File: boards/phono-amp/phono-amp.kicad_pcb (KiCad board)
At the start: 2 copper layers, 28 parts, among them J1 Conn_Coaxial, J2 Conn_01x06_Male, J3 Conn_Coaxial, U1 6DJ8

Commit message: layout underway
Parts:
- moved J2 173.4 mm to (72.4, 65.8), turned to 90 degrees
- moved R12 94.9 mm to (170.2, 135.9), turned to 90 degrees
- moved C2 56.4 mm to (152.4, 87.6)
- moved R6B1 54.2 mm to (152.4, 76.2), turned to 90 degrees
- moved R6A1 42.6 mm to (160.0, 66.0), turned to 270 degrees
- moved C7 40.2 mm to (95.2, 80.0), turned to 270 degrees
- moved R7 39.2 mm to (145.8, 77.5), turned to 90 degrees
- moved R5 35.4 mm to (116.8, 69.8), turned to 270 degrees
- moved R8 33.6 mm to (139.7, 81.3)
- moved R11 31.4 mm to (195.6, 123.2)
- moved C4 31.4 mm to (184.2, 101.6)
- moved C6 31.4 mm to (154.9, 108.0)
- moved R1 31.4 mm to (71.1, 118.1)
- moved R10 31.4 mm to (163.8, 99.1)
- moved R2 31.4 mm to (95.2, 102.9)
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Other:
- board outline added: 152.4 x 115.6 mm

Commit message: Amp PCB done?
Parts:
- added H1: MountingHole_Pad, MountingHole:MountingHole_4.3mm_M4_ISO7380_Pad, F.Cu at (74.9, 41.9)
- added H2: MountingHole_Pad, MountingHole:MountingHole_4.3mm_M4_ISO7380_Pad, F.Cu at (217.2, 41.9)
- added H3: MountingHole_Pad, MountingHole:MountingHole_4.3mm_M4_ISO7380_Pad, F.Cu at (74.9, 147.3)
- added H4: MountingHole_Pad, MountingHole:MountingHole_4.3mm_M4_ISO7380_Pad, F.Cu at (217.2, 147.3)
- added H5: MountingHole_Pad, MountingHole:MountingHole_4.3mm_M4_ISO7380_Pad, F.Cu at (74.9, 72.4)
- added JP1: 6DJ8, Connector_PinHeader_2.54mm:PinHeader_1x03_P2.54mm_Vertical, F.Cu at (127.0, 102.9)
- J1: value Conn_Coaxial -> INPUT
- J2: value Conn_01x06_Male -> POWER
- J3: value Conn_Coaxial -> OUTPUT
- R5: value 82k5 1/4W 1% -> 82.5k
- R6A1: value 10k7 1/4W 1% -> 10k
- R6B1: value 100 1/4W 1% -> 100
- R7: value 470k 1/4W -> 470k
- R8: value 500R 1/4W -> 500
- moved J2 84.6 mm to (99.1, 146.1), turned to 0 degrees
- moved R12 68.6 mm to (101.6, 133.3), turned to 0 degrees
- moved R6A1 40.8 mm to (120.7, 76.8), turned to 90 degrees
- moved R6B1 38.7 mm to (114.9, 66.7), turned to 270 degrees
- moved C1A1 35.0 mm to (151.8, 67.3)
- moved C3 34.9 mm to (163.2, 77.5)
- moved C1B1 34.4 mm to (143.5, 67.3)
- moved C1C1 33.1 mm to (135.9, 67.3)
- moved C2 32.0 mm to (127.6, 67.3), turned to 270 degrees
- moved R7 17.6 mm to (149.9, 94.6), turned to 0 degrees
- moved R10 17.3 mm to (158.8, 115.6), turned to 90 degrees
- moved R2 15.9 mm to (111.1, 102.9)
- moved R11 15.8 mm to (185.4, 111.1), turned to 0 degrees
- moved R3 15.7 mm to (95.9, 113.0), turned to 0 degrees
- moved R1 15.4 mm to (73.0, 102.9), turned to 0 degrees
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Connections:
- U1 pad 10: (no net) -> Net-(JP1-Pad2)
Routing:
- net Earth_Protective: track 0.00 -> 344.7 mm
- net VBUS: track 0.00 -> 286.9 mm
- net Net-(C2-Pad1): track 0.00 -> 61.2 mm
- net Net-(C4-Pad2): track 0.00 -> 52.8 mm
- net GND: track 0.00 -> 48.4 mm
- net Net-(J2-Pad6): track 0.00 -> 40.8 mm
- net Net-(J2-Pad4): track 0.00 -> 40.5 mm
- net Net-(C4-Pad1): track 0.00 -> 38.5 mm
- net Net-(C1A1-Pad1): track 0.00 -> 35.5 mm
- net Net-(C6-Pad1): track 0.00 -> 34.9 mm
- net Net-(J1-Pad1): track 0.00 -> 26.7 mm
- net Net-(C5-Pad1): track 0.00 -> 24.0 mm
- net Net-(C7-Pad1): track 0.00 -> 23.6 mm
- net Net-(C3-Pad1): track 0.00 -> 19.0 mm
- net Net-(R8-Pad1): track 0.00 -> 18.4 mm
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- added copper zone on B.Cu, net GND
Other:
- board text added: "6DJ8 Phono Stage Design: RJM Audio"
- board text added: "PCB: E. Hazen 2021-05-02"

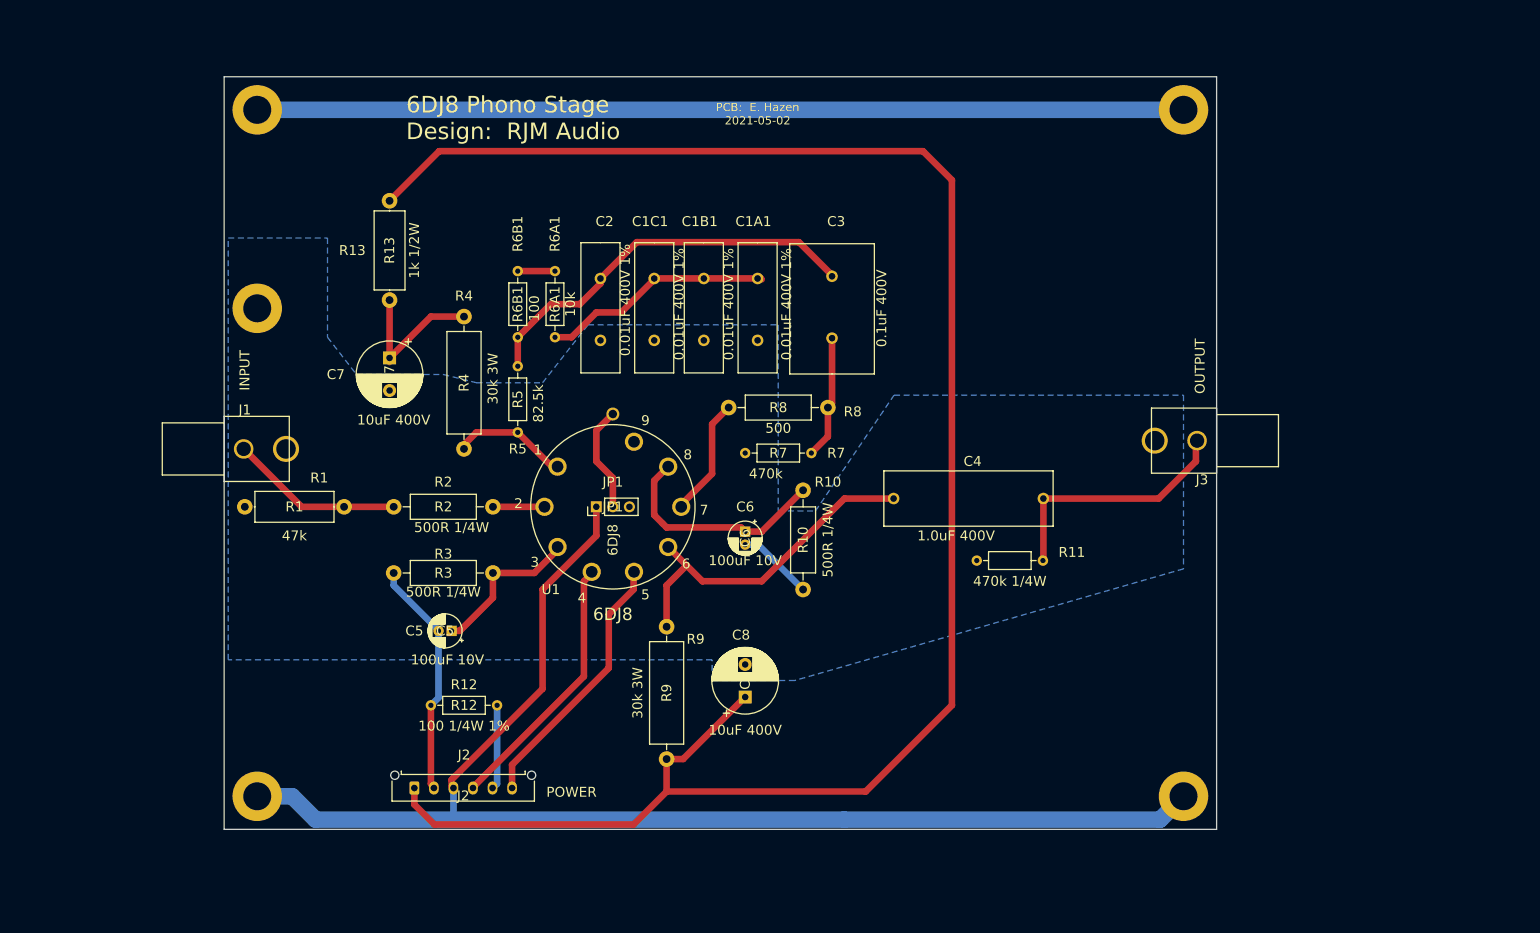
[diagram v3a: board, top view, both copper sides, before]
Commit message: resize boards
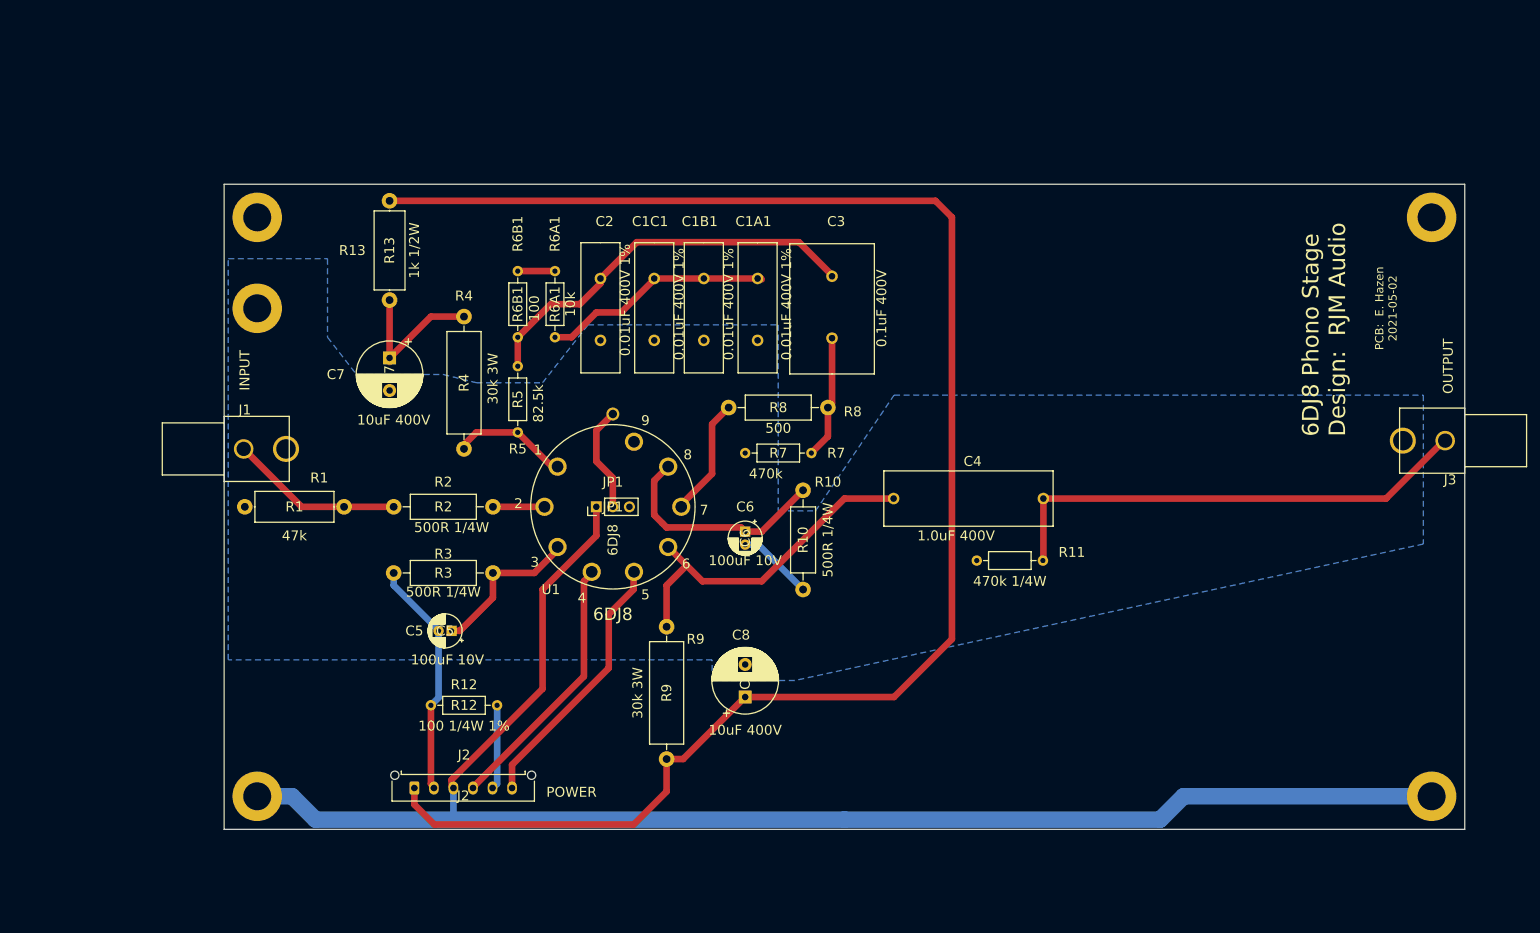
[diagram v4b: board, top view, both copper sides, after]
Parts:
- moved H2 41.5 mm to (255.3, 58.4)
- moved H4 38.1 mm to (255.3, 147.3)
- moved J3 38.1 mm to (260.4, 92.7)
- moved H1 16.5 mm to (74.9, 58.4)
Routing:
- net Earth_Protective: track 344.7 -> 240.6 mm
- net Net-(C4-Pad1): track 38.5 -> 74.8 mm
- net VBUS: track 286.9 -> 253.3 mm
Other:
- board size 152.4 x 115.6 mm -> 190.5 x 99.1 mm
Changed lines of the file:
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@@
     (thickness 1.6)
     (drawings 6)
-    (tracks 110)
+    (tracks 108)
     (zones 0)
     (modules 34)
@@
   )
   (setup
-    (last_trace_width 0.25)
+    (last_trace_width 1.016)
     (user_trace_width 0.381)
     (user_trace_width 0.635)
@@
     (add_net "Net-(R8-Pad1)")
     (add_net VBUS)
+  )
+  (module my-connectors:rca-single-klpx (layer F.Cu)
+    (at 260.35 92.71 180)
+    (fp_text reference J3 (at 2.25 -6) (layer F.SilkS)
+      (effects (font (size 1.524 1.524) (thickness 0.15)))
+    )
+    (fp_text value OUTPUT (at 2.54 11.43 90) (layer F.SilkS)
+      (effects (font (size 1.524 1.524) (thickness 0.15)))
+    )
+    (fp_line (start 0 -5) (end 0 5) (layer F.SilkS) (width 0.12))
+    (fp_line (start 0 5) (end 10 5) (layer F.SilkS) (width 0.12))
+    (fp_line (start 10 -5) (end 0 -5) (layer F.SilkS) (width 0.12))
+    (fp_line (start 10 -5) (end 10 5) (layer F.SilkS) (width 0.12))
+    (fp_line (start 0 -4) (end -9.5 -4) (layer F.SilkS) (width 0.12))
+    (fp_line (start -9.5 -4) (end -9.5 4) (layer F.SilkS) (width 0.12))
+    (fp_line (start -9.5 4) (end 0 4) (layer F.SilkS) (width 0.12))
+    (pad 2 thru_hole circle (at 9.5 0 180) (size 4 4) (drill 3) (layers *.Cu *.Mask)
+      (net 1 GND))
+    (pad 1 thru_hole circle (at 3 0 180) (size 3 3) (drill 2.2) (layers *.Cu *.Mask)
+      (net 4 "Net-(C4-Pad1)"))
   )
   (module my-capacitors:CAP_L20_W6.4_P9.5 (layer F.Cu)
@@
     )
   )
-  (module my-connectors:rca-single-klpx (layer F.Cu)
-    (at 222.25 92.71 180)
-    (fp_text reference J3 (at 2.25 -6) (layer F.SilkS)
-      (effects (font (size 1.524 1.524) (thickness 0.15)))
-    )
-    (fp_text value OUTPUT (at 2.54 11.43 90) (layer F.SilkS)
-      (effects (font (size 1.524 1.524) (thickness 0.15)))
-    )
-    (fp_line (start 0 -5) (end 0 5) (layer F.SilkS) (width 0.12))
-    (fp_line (start 0 5) (end 10 5) (layer F.SilkS) (width 0.12))
-    (fp_line (start 10 -5) (end 0 -5) (layer F.SilkS) (width 0.12))
-    (fp_line (start 10 -5) (end 10 5) (layer F.SilkS) (width 0.12))
-    (fp_line (start 0 -4) (end -9.5 -4) (layer F.SilkS) (width 0.12))
-    (fp_line (start -9.5 -4) (end -9.5 4) (layer F.SilkS) (width 0.12))
-    (fp_line (start -9.5 4) (end 0 4) (layer F.SilkS) (width 0.12))
-    (pad 2 thru_hole circle (at 9.5 0 180) (size 4 4) (drill 3) (layers *.Cu *.Mask)
-      (net 1 GND))
-    (pad 1 thru_hole circle (at 3 0 180) (size 3 3) (drill 2.2) (layers *.Cu *.Mask)
-      (net 4 "Net-(C4-Pad1)"))
-  )
   (module Resistor_THT:R_Axial_DIN0414_L11.9mm_D4.5mm_P15.24mm_Horizontal (layer F.Cu)
     (at 73.025 102.87)
@@
   )
   (module MountingHole:MountingHole_4.3mm_M4_ISO7380_Pad (layer F.Cu)
-    (at 74.93 41.91)
+    (at 74.93 58.42)
     (descr "Mounting Hole 4.3mm, M4, ISO7380")
     (tags "mounting hole 4.3mm m4 iso7380")
@@
   )
   (module MountingHole:MountingHole_4.3mm_M4_ISO7380_Pad (layer F.Cu)
-    (at 217.17 41.91)
+    (at 255.27 58.42)
     (descr "Mounting Hole 4.3mm, M4, ISO7380")
     (tags "mounting hole 4.3mm m4 iso7380")
@@
   )
   (module MountingHole:MountingHole_4.3mm_M4_ISO7380_Pad (layer F.Cu)
-    (at 217.17 147.32)
+    (at 255.27 147.32)
     (descr "Mounting Hole 4.3mm, M4, ISO7380")
     (tags "mounting hole 4.3mm m4 iso7380")
@@
     )
   )
-  (gr_text "PCB:  E. Hazen\n2021-05-02" (at 151.765 42.545) (layer F.SilkS)
+  (gr_text "PCB:  E. Hazen\n2021-05-02" (at 248.285 72.39 90) (layer F.SilkS)
     (effects (font (size 1.27 1.27) (thickness 0.2032)))
   )
-  (gr_text "6DJ8 Phono Stage\nDesign:  RJM Audio" (at 97.79 43.18) (layer F.SilkS)
+  (gr_text "6DJ8 Phono Stage\nDesign:  RJM Audio" (at 238.76 92.075 90) (layer F.SilkS)
     (effects (font (size 2.54 2.54) (thickness 0.2032)) (justify left))
   )
-  (gr_line (start 222.25 36.83) (end 69.85 36.83) (layer Edge.Cuts) (width 0.05))
-  (gr_line (start 222.25 152.4) (end 222.25 36.83) (layer Edge.Cuts) (width 0.05))
-  (gr_line (start 69.85 152.4) (end 222.25 152.4) (layer Edge.Cuts) (width 0.05))
-  (gr_line (start 69.85 36.83) (end 69.85 152.4) (layer Edge.Cuts) (width 0.05))
+  (gr_line (start 260.35 53.34) (end 69.85 53.34) (layer Edge.Cuts) (width 0.05))
+  (gr_line (start 260.35 152.4) (end 260.35 53.34) (layer Edge.Cuts) (width 0.05))
+  (gr_line (start 69.85 152.4) (end 260.35 152.4) (layer Edge.Cuts) (width 0.05))
+  (gr_line (start 69.85 53.34) (end 69.85 152.4) (layer Edge.Cuts) (width 0.05))
   (segment (start 102.775 121.92) (end 102.775 132.175) (width 1.016) (layer B.Cu) (net 1))
   (segment (start 102.775 132.175) (end 101.6 133.35) (width 1.016) (layer B.Cu) (net 1))
@@
   (segment (start 162.56 87.63) (end 162.56 92.075) (width 1.016) (layer F.Cu) (net 3))
   (segment (start 162.56 92.075) (end 160.02 94.615) (width 1.016) (layer F.Cu) (net 3))
-  (segment (start 195.65 101.6) (end 213.36 101.6) (width 1.016) (layer F.Cu) (net 4))
-  (segment (start 213.36 101.6) (end 219.075 95.885) (width 1.016) (layer F.Cu) (net 4))
-  (segment (start 219.075 95.885) (end 219.075 92.71) (width 1.016) (layer F.Cu) (net 4))
   (segment (start 195.65 101.6) (end 195.65 111.055) (width 1.016) (layer F.Cu) (net 4))
   (segment (start 195.65 111.055) (end 195.58 111.125) (width 1.016) (layer F.Cu) (net 4))
+  (segment (start 195.65 101.6) (end 248.285 101.6) (width 1.016) (layer F.Cu) (net 4))
+  (segment (start 248.285 101.6) (end 257.175 92.71) (width 1.016) (layer F.Cu) (net 4))
   (segment (start 143.292933 114.3) (end 152.4 114.3) (width 1.016) (layer F.Cu) (net 5))
   (segment (start 152.4 114.3) (end 165.1 101.6) (width 1.016) (layer F.Cu) (net 5))
@@
   (segment (start 137.795 141.605) (end 140.335 141.605) (width 1.016) (layer F.Cu) (net 9))
   (segment (start 140.335 141.605) (end 149.86 132.08) (width 1.016) (layer F.Cu) (net 9))
-  (segment (start 95.25 55.88) (end 102.87 48.26) (width 1.016) (layer F.Cu) (net 9))
-  (segment (start 102.87 48.26) (end 177.165 48.26) (width 1.016) (layer F.Cu) (net 9))
-  (segment (start 177.165 48.26) (end 181.61 52.705) (width 1.016) (layer F.Cu) (net 9))
-  (segment (start 181.61 52.705) (end 181.61 133.35) (width 1.016) (layer F.Cu) (net 9))
-  (segment (start 168.37301 146.58699) (end 137.795 146.58699) (width 1.016) (layer F.Cu) (net 9))
-  (segment (start 181.61 133.35) (end 168.37301 146.58699) (width 1.016) (layer F.Cu) (net 9))
   (segment (start 99.06 148.59) (end 99.06 146.05) (width 1.016) (layer F.Cu) (net 9))
+  (segment (start 95.25 55.88) (end 179.07 55.88) (width 1.016) (layer F.Cu) (net 9))
+  (segment (start 179.07 55.88) (end 181.61 58.42) (width 1.016) (layer F.Cu) (net 9))
+  (segment (start 181.61 58.42) (end 181.61 123.19) (width 1.016) (layer F.Cu) (net 9))
+  (segment (start 181.61 123.19) (end 172.72 132.08) (width 1.016) (layer F.Cu) (net 9))
+  (segment (start 172.72 132.08) (end 149.86 132.08) (width 1.016) (layer F.Cu) (net 9))
   (segment (start 120.65 76.835) (end 123.19 76.835) (width 1.016) (layer F.Cu) (net 10))
   (segment (start 123.19 76.835) (end 127 73.025) (width 1.016) (layer F.Cu) (net 10))
@@
   (segment (start 81.74 102.87) (end 88.265 102.87) (width 1.016) (layer F.Cu) (net 11))
   (segment (start 88.265 102.87) (end 95.885 102.87) (width 1.016) (layer F.Cu) (net 11))
-  (segment (start 74.93 41.91) (end 217.17 41.91) (width 2.54) (layer B.Cu) (net 12))
   (segment (start 80.304011 147.32) (end 83.889001 150.90499) (width 2.54) (layer B.Cu) (net 12))
   (segment (start 74.93 147.32) (end 80.304011 147.32) (width 2.54) (layer B.Cu) (net 12))
-  (segment (start 165.1 150.90499) (end 213.58501 150.90499) (width 2.54) (layer B.Cu) (net 12))
-  (segment (start 213.58501 150.90499) (end 217.17 147.32) (width 2.54) (layer B.Cu) (net 12))
   (segment (start 127 102.87) (end 127 107.315) (width 1.016) (layer F.Cu) (net 12))
   (segment (start 127 107.315) (end 118.745 115.57) (width 1.016) (layer F.Cu) (net 12))
@@
   (segment (start 105.06 150.845) (end 105.00001 150.90499) (width 1.016) (layer B.Cu) (net 12))
   (segment (start 105.06 146.05) (end 105.06 150.845) (width 1.016) (layer B.Cu) (net 12))
+  (segment (start 83.889001 150.90499) (end 105.00001 150.90499) (width 2.54) (layer B.Cu) (net 12))
   (segment (start 105.00001 150.90499) (end 165.1 150.90499) (width 2.54) (layer B.Cu) (net 12))
-  (segment (start 83.889001 150.90499) (end 105.00001 150.90499) (width 2.54) (layer B.Cu) (net 12))
+  (segment (start 213.58501 150.90499) (end 217.17 147.32) (width 2.54) (layer B.Cu) (net 12))
+  (segment (start 165.1 150.90499) (end 213.58501 150.90499) (width 2.54) (layer B.Cu) (net 12))
+  (segment (start 217.17 147.32) (end 255.27 147.32) (width 2.54) (layer B.Cu) (net 12))
   (segment (start 125.095 128.905) (end 125.095 114.3) (width 1.016) (layer F.Cu) (net 13))
   (segment (start 108.06 145.94) (end 125.095 128.905) (width 1.016) (layer F.Cu) (net 13))
@@
         (xy 85.725 76.835) (xy 90.17 82.55) (xy 103.505 82.55) (xy 108.585 83.82) (xy 118.745 83.82)
         (xy 125.73 74.93) (xy 154.94 74.93) (xy 154.94 103.505) (xy 160.655 103.505) (xy 172.72 85.725)
-        (xy 217.17 85.725) (xy 217.17 112.395) (xy 157.48 129.54) (xy 144.78 129.54) (xy 144.78 126.365)
-        (xy 70.485 126.365) (xy 70.485 61.595) (xy 85.725 61.595)
+        (xy 254 85.725) (xy 254 108.585) (xy 157.48 129.54) (xy 144.78 129.54) (xy 144.78 126.365)
+        (xy 70.485 126.365) (xy 70.485 64.77) (xy 85.725 64.77)
       )
     )
